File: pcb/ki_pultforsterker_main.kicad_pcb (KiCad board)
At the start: 2 copper layers, 180 x 100 mm, 243 parts, among them J1 24V IN, J10 LED-RINGER, J11 PC1, J12 PC2, J13 TFT, J15 USB1, J16 USB2, J17 USB3, J18 USB4, J19 USB PI, J2 SPK L, J20 AUX2, J21 PWR BAK, J22 EXP, J23 HODETLF, J3 SPK R, J4 AUX1, J5 RPi 40-pin, J6 5V -> PI, J7 KNAPPER, J8 ENCODER, J9 OLED, K1 SRD-05VDC-SL-C, Q10 AO3401A, Q2 AO3400A, Q3 AO3400A, Q4 AO3400A, Q5 AO3400A, Q6 AO3400A, Q7 AO3400A, Q8 AO3401A, Q9 AO3400A, U1 TPS54560BDDA, U10 PCM1808PW, U11 PCM2900CDB, U12 MCP23017-E/SS, U13 TPA6132A2RTER, U2 AMS1117-3.3, U3 LM2662MX, U4 PCM5102APW, U5 PGA2311UA, U6 TPA3116D2DAD, U7 FE1.1s, U8 TS3USB221, U9 AMS1117-3.3, X1 12.288MHz, Y1 12MHz, Y2 12MHz

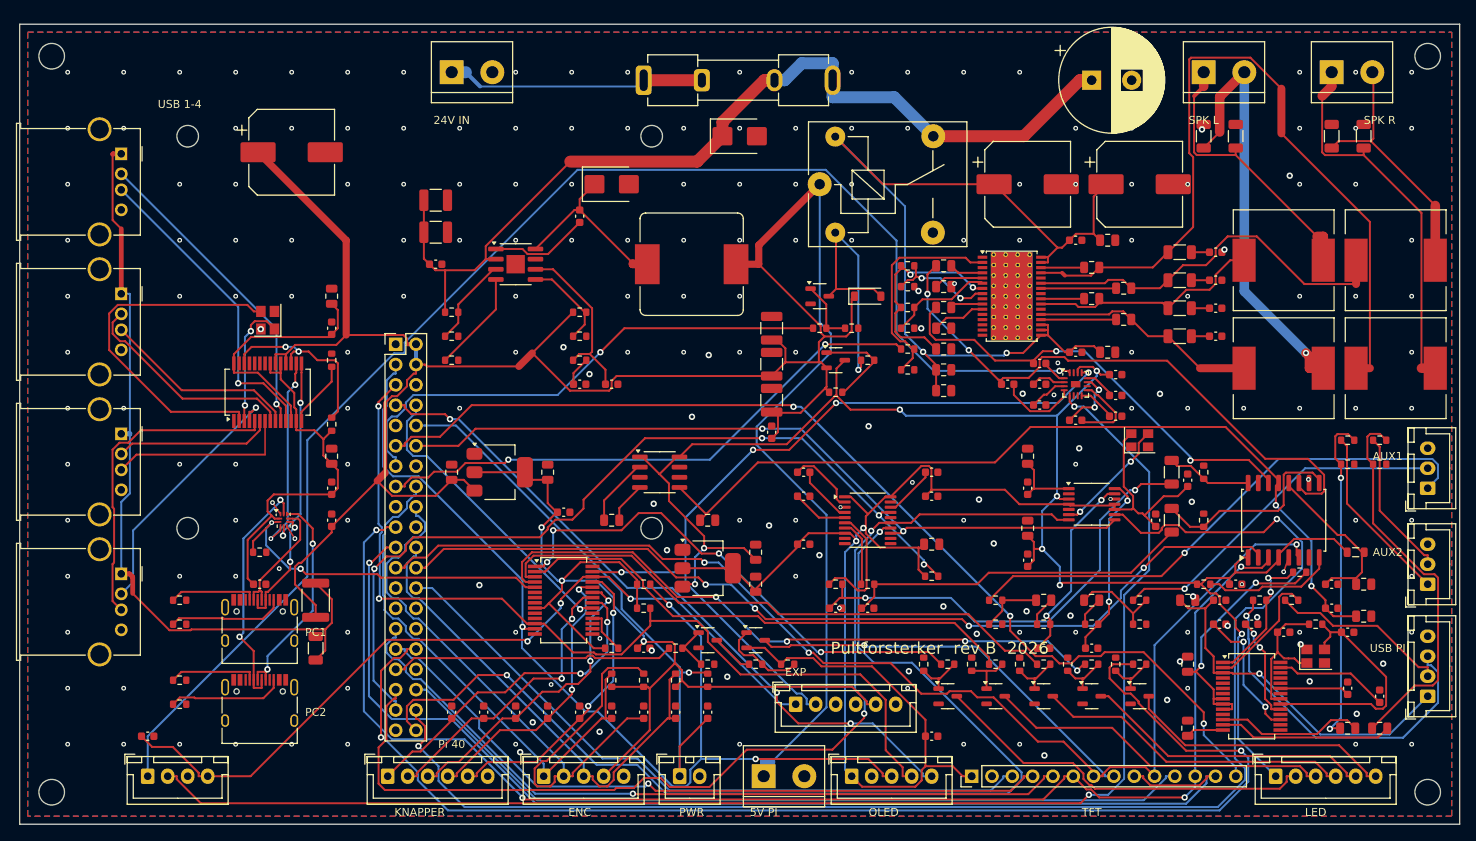
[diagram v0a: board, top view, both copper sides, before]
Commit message: PCB rev B: endelig ruting, gerbere, BOM og DRC etter sikkerhetsgjennomgang
DRC: ingen klaringsfeil, ingen ukoblede nett, alle GND-pads koblet, jordplanet i én del (186 stitching-/bro-vias).
Gjenstår bare silk-advarsler og små courtyard-overlapp.

Co-Authored-By: Claude Fable 5.1 <noreply@anthropic.com>
Claude-Session: https://claude.ai/code/session_01FaJKmYinw8SWRobKXBRYpt
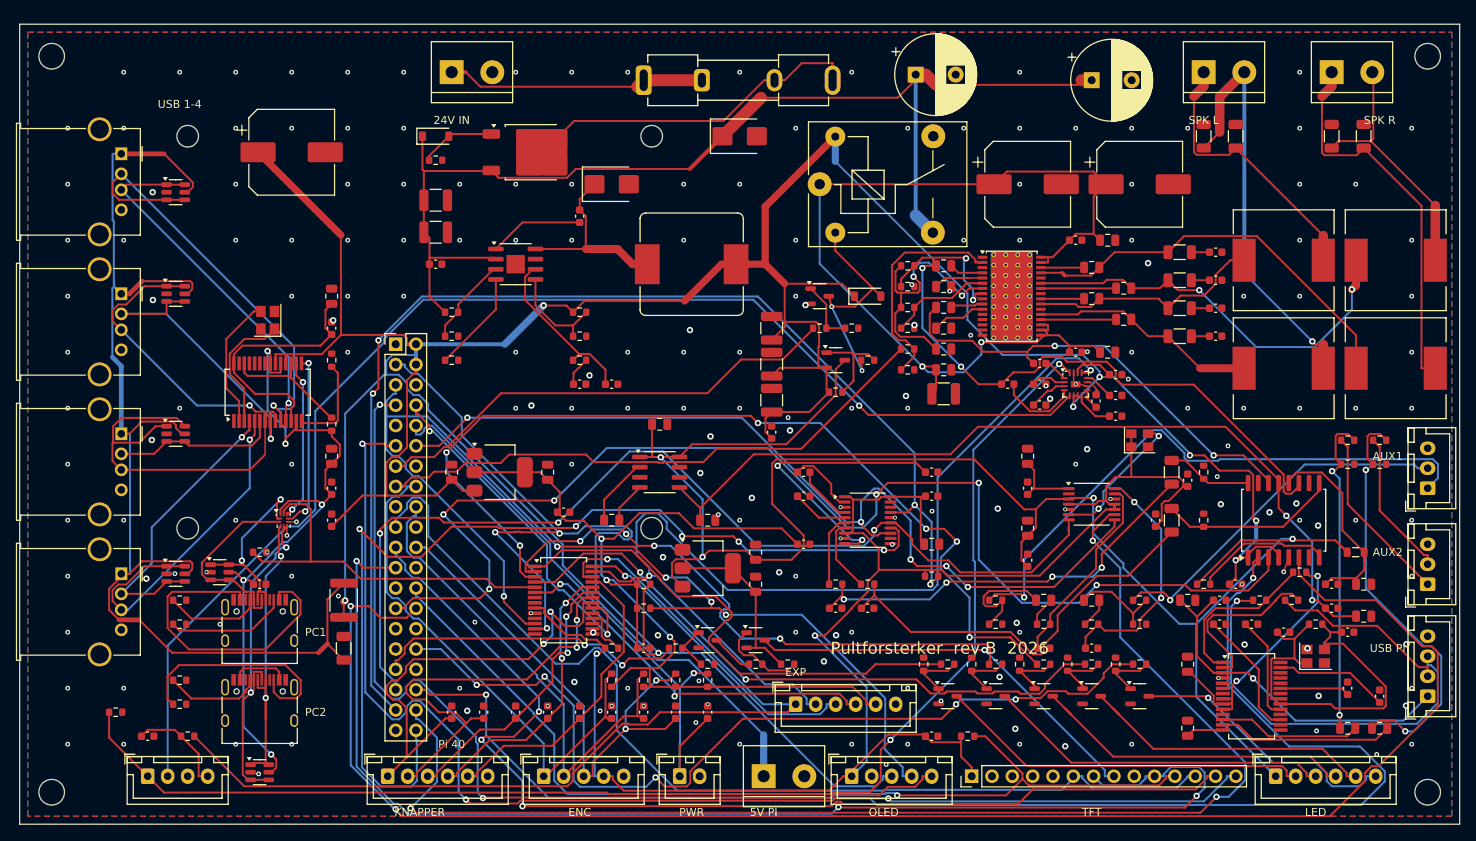
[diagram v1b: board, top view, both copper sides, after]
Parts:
- added C109: 10u, C_0805_2012Metric, F.Cu at (80.0, 50.0)
- added C110: 1000u/35V h<=16, CP_Radial_D10.0mm_P5.00mm, F.Cu at (112.0, 6.30)
- added D10: USBLC6-2SC6, SOT-23-6, F.Cu at (25.0, 68.5)
- added D11: USBLC6-2SC6, SOT-23-6, F.Cu at (30.0, 93.5)
- added D5: BZT52C12 12V, D_SOD-123, F.Cu at (52.0, 14.0)
- added D6: USBLC6-2SC6, SOT-23-6, F.Cu at (19.5, 21.0)
- added D7: USBLC6-2SC6, SOT-23-6, F.Cu at (19.5, 33.7)
- added D8: USBLC6-2SC6, SOT-23-6, F.Cu at (19.5, 51.2)
- added D9: USBLC6-2SC6, SOT-23-6, F.Cu at (19.5, 68.7)
- added Q11: P-MOSFET 60V 20A (AOD409), TO-252-2, F.Cu at (64.0, 16.0)
- added R76: 10k, R_0603_1608Metric, F.Cu at (12.0, 86.0)
- added R77: 10k, R_0603_1608Metric, F.Cu at (21.0, 89.0)
- added R78: 10k, R_0603_1608Metric, F.Cu at (118.5, 89.0)
- added R79: 100k, R_0603_1608Metric, F.Cu at (52.0, 17.0)
- C1: value 2200u/35V -> 1000u/35V h<=16; footprint CP_Radial_D13.0mm_P5.00mm -> CP_Radial_D10.0mm_P5.00mm
- C43: value 10u/50V -> 4.7u/50V; footprint C_0805_2012Metric -> C_1210_3225Metric
- D1: value SMBJ33A -> SMBJ28A
- R1: value 150k -> 330k
- R4: value 53.6k -> 56k
- U1: value TPS54560BDDA -> TPS54560DDAR
- U10: value PCM1808PW -> PCM1808PWR
- U4: value PCM5102APW -> PCM5102APWR
- U6: value TPA3116D2DAD -> TPA3116D2DADR
- U8: value TS3USB221 -> TS3USB221RSER
- moved C103 3.50 mm to (134.6, 47.1), turned to -90 degrees
- moved C71 3.50 mm to (40.5, 78.0)
- moved F2 3.50 mm to (40.5, 72.0)
- moved C43 0.40 mm to (115.5, 46.2)
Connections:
- C100 pad 1: 5V_SW -> 5V
- C108 pad 1: EXP_A5 -> HP_DET
- C20 pad 1: 3V3_SW -> 3V3
- C21 pad 1: 3V3_SW -> 3V3
- C22 pad 1: 3V3_SW -> 3V3
- C27 pad 1: 5V_SW -> 5V
- C77 pad 1: 3V3_SW -> 3V3
- C82 pad 1: 3V3_SW -> 3V3
- C99 pad 1: 3V3_SW -> 3V3
- F1 pad 2: VIN24 -> 24V_F
- J11 pad A4: (no net) -> PC1_VBUS
- J11 pad A9: (no net) -> PC1_VBUS
- J11 pad B4: (no net) -> PC1_VBUS
- J11 pad B9: (no net) -> PC1_VBUS
- J12 pad A4: (no net) -> PC2_VBUS
- J12 pad A9: (no net) -> PC2_VBUS
- J12 pad B4: (no net) -> PC2_VBUS
- J12 pad B9: (no net) -> PC2_VBUS
- J13 pad 1: 3V3_SW -> 3V3
- J13 pad 3: TFT_CS -> (no net)
- J13 pad 4: TFT_RST -> (no net)
- J13 pad 5: TFT_DC -> (no net)
- J13 pad 9: SPI_MISO -> (no net)
- J22 pad 3: (no net) -> EXP_A7
- J22 pad 4: (no net) -> EXP_B5
- J22 pad 6: (no net) -> GND
- J23 pad 4: EXP_A5 -> HP_DET
- J5 pad 24: SPI_CS -> (no net)
- J5 pad 26: TFT_CS -> TOUCH_CS
- J5 pad 27: (no net) -> PGA_SDI
- J5 pad 28: (no net) -> PGA_SCLK
- J5 pad 29: TFT_DC -> (no net)
- J5 pad 31: TFT_RST -> (no net)
- J5 pad 36: TOUCH_CS -> PGA_CS
- J9 pad 1: 3V3_SW -> 3V3
- K1 pad 1: 5V -> 24V_AMP
- K1 pad 3: (no net) -> VIN24
- K1 pad 4: VIN24 -> (no net)
- K1 pad 5: 24V_AMP -> 5V
- R7 pad 1: 3V3_SW -> 3V3
- U10 pad 10: 3V3_SW -> 3V3
- U10 pad 11: 3V3_SW -> 3V3
- U10 pad 4: 3V3_SW -> 3V3
- U12 pad 28: (no net) -> EXP_A7
- U12 pad 6: (no net) -> EXP_B5
- U13 pad 14: 5V_SW -> 5V
- U13 pad 6: GND -> 5V
- U13 pad 7: GND -> 5V
- U4 pad 1: 3V3_SW -> 3V3
- U4 pad 10: GND -> DAC_LDOO
- U4 pad 18: DAC_LDOO -> GND
- U4 pad 20: 3V3_SW -> 3V3
- U4 pad 8: 3V3_SW -> 3V3
- U5 pad 1: 5V_SW -> 5V
- U5 pad 2: SPI_CS -> PGA_CS
- U5 pad 3: SPI_MOSI -> PGA_SDI
- U5 pad 4: 5V_SW -> 5V
- U5 pad 6: SPI_SCLK -> PGA_SCLK
- U8 pad 1: USB_VD33 -> PC1_DP
- U8 pad 10: GND -> USB_VD33
- U8 pad 2: USB_SEL -> PC1_DM
- U8 pad 3: USB_UP_DP -> PC2_DP
- U8 pad 4: USB_UP_DM -> PC2_DM
- U8 pad 6: PC1_DP -> GND
- U8 pad 7: PC1_DM -> USB_UP_DM
- U8 pad 8: PC2_DP -> USB_UP_DP
- U8 pad 9: PC2_DM -> USB_SEL
- X1 pad 1: (no net) -> 3V3
- X1 pad 4: 3V3_SW -> 3V3
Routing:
- net 3V3: track 128.3 -> 336.3 mm, vias 3 -> 5
- net PGA_SCLK: track 0.00 -> 204.2 mm, vias 0 -> 2
- net PGA_CS: track 0.00 -> 174.4 mm, vias 0 -> 2
- net 3V3_SW: track 190.2 -> 22.6 mm, vias 2 -> 0
- net PGA_SDI: track 0.00 -> 154.7 mm, vias 0 -> 6
- net 5V: track 313.9 -> 433.9 mm, vias 0 -> 7
- net SPI_CS: track 115.7 -> 0.00 mm, vias 4 -> 0
- net TFT_DC: track 95.8 -> 0.00 mm, vias 1 -> 0
- net TFT_RST: track 89.0 -> 0.00 mm, vias 1 -> 0
- net TFT_CS: track 85.9 -> 0.00 mm
- net 5V_USB: track 97.5 -> 149.7 mm
- net 24V_F: track 0.00 -> 50.5 mm
- net EXP_B5: track 0.00 -> 47.6 mm, vias 0 -> 2
- net OUTPR: track 97.3 -> 50.8 mm
- net LED_PWR_G: track 157.3 -> 111.9 mm, vias 2 -> 5
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
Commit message: PCB rev B: endelig ruting med GND som rutet nett + plan, NTC-overtemperaturvakt, gerbere/BOM/DRC
DRC: 0 klaringsfeil, 0 hullfeil, 0 ukoblede, jordplanet i én del. Gjenstår silk-advarsler og små courtyard-overlapp.

Co-Authored-By: Claude Fable 5.1 <noreply@anthropic.com>
Claude-Session: https://claude.ai/code/session_01FaJKmYinw8SWRobKXBRYpt
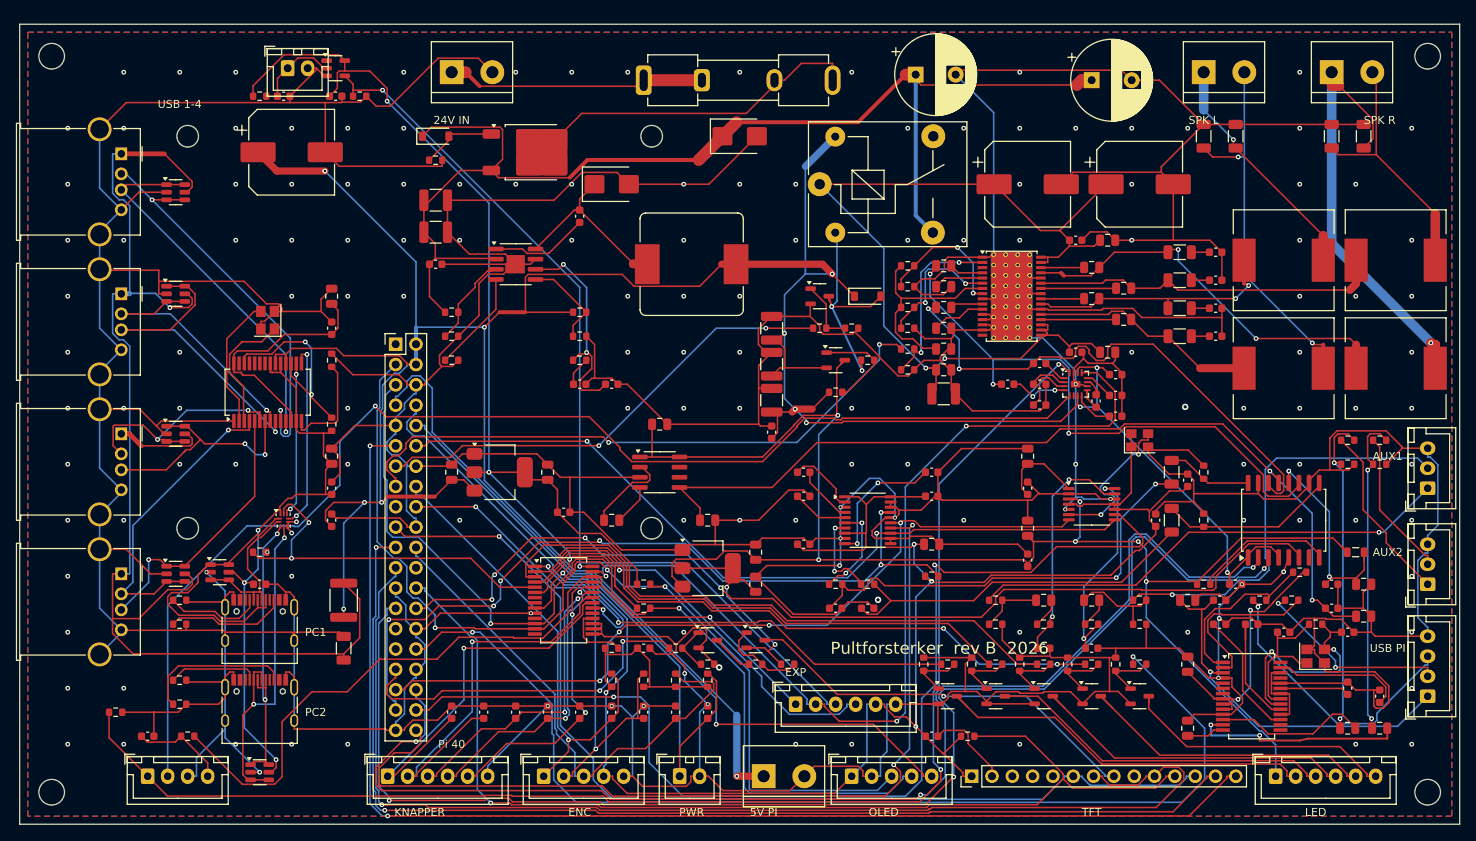
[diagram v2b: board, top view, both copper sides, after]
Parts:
- added C111: 100n, C_0603_1608Metric, F.Cu at (39.5, 9.00)
- added C112: 100n, C_0603_1608Metric, F.Cu at (33.0, 9.00)
- added J24: NTC, JST_XH_B2B-XH-A_1x02_P2.50mm_Vertical, F.Cu at (33.5, 5.50)
- added R81: 3.3k, R_0603_1608Metric, F.Cu at (30.0, 9.00)
- added R82: 100k, R_0603_1608Metric, F.Cu at (42.5, 9.00)
- added U14: 74LVC1G14, SOT-23-5, F.Cu at (39.5, 5.50)
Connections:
- J11 pad A4: PC1_VBUS -> PC1_VBUS_A
- J11 pad A9: PC1_VBUS -> PC1_VBUS_B
- J11 pad B4: PC1_VBUS -> PC1_VBUS_B
- J11 pad B9: PC1_VBUS -> PC1_VBUS_A
- J12 pad A4: PC2_VBUS -> PC2_VBUS_A
- J12 pad A9: PC2_VBUS -> PC2_VBUS_B
- J12 pad B4: PC2_VBUS -> PC2_VBUS_B
- J12 pad B9: PC2_VBUS -> PC2_VBUS_A
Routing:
- net GND: track 6.18 -> 1674.6 mm, vias 204 -> 154
- net EXP_A7: track 38.8 -> 117.5 mm, vias 1 -> 2
- net PGA_SCLK: track 204.2 -> 125.8 mm, vias 2 -> 4
- net DAC_XSMT: track 147.4 -> 97.4 mm, vias 4 -> 6
- net 3V3: track 336.3 -> 386.0 mm, vias 5 -> 8
- net LED_AUX_G: track 117.1 -> 75.3 mm, vias 6 -> 0
- net PC1_VBUS: track 39.7 -> 0.00 mm
- net I2S_ADC: track 163.7 -> 135.1 mm, vias 3 -> 2
- net I2S_LRCK: track 125.3 -> 99.9 mm, vias 3 -> 4
- net OLED_RES: track 120.2 -> 95.6 mm, vias 2 -> 1
- net 5V_SW: track 221.6 -> 198.2 mm, vias 4 -> 6
- net LED_PWR_G: track 111.9 -> 134.9 mm, vias 5 -> 2
- net DAC_LDOO: track 35.9 -> 16.7 mm
- net EXP_A5: track 119.8 -> 101.4 mm
- net 5V: track 433.9 -> 416.0 mm, vias 7 -> 13
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
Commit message: PCB rev B: ferdig rutet – DRC uten klarings-, kortslutnings-, kant- eller koblingsfeil
Full ny Freerouting-kjøring med låst strømskinne (24 V inn → sikring → Q11 → relé → TPA3116,
5 V buck → C8–C11 → J6/Pi-header). Flaskehalser: 24V_IN 2,0, 24V_F 1,85, VIN24 1,0, 5 V til Pi 1,5 mm.
Gjenstår i DRC: kun silk/courtyard-varsler, 11 «starved thermal» på THT-GND-pads som også har rutet GND-spor,
og 199 bibliotekmeldinger (footprints er innebygd).

Co-Authored-By: Claude Fable 5.1 <noreply@anthropic.com>
Claude-Session: https://claude.ai/code/session_01FaJKmYinw8SWRobKXBRYpt
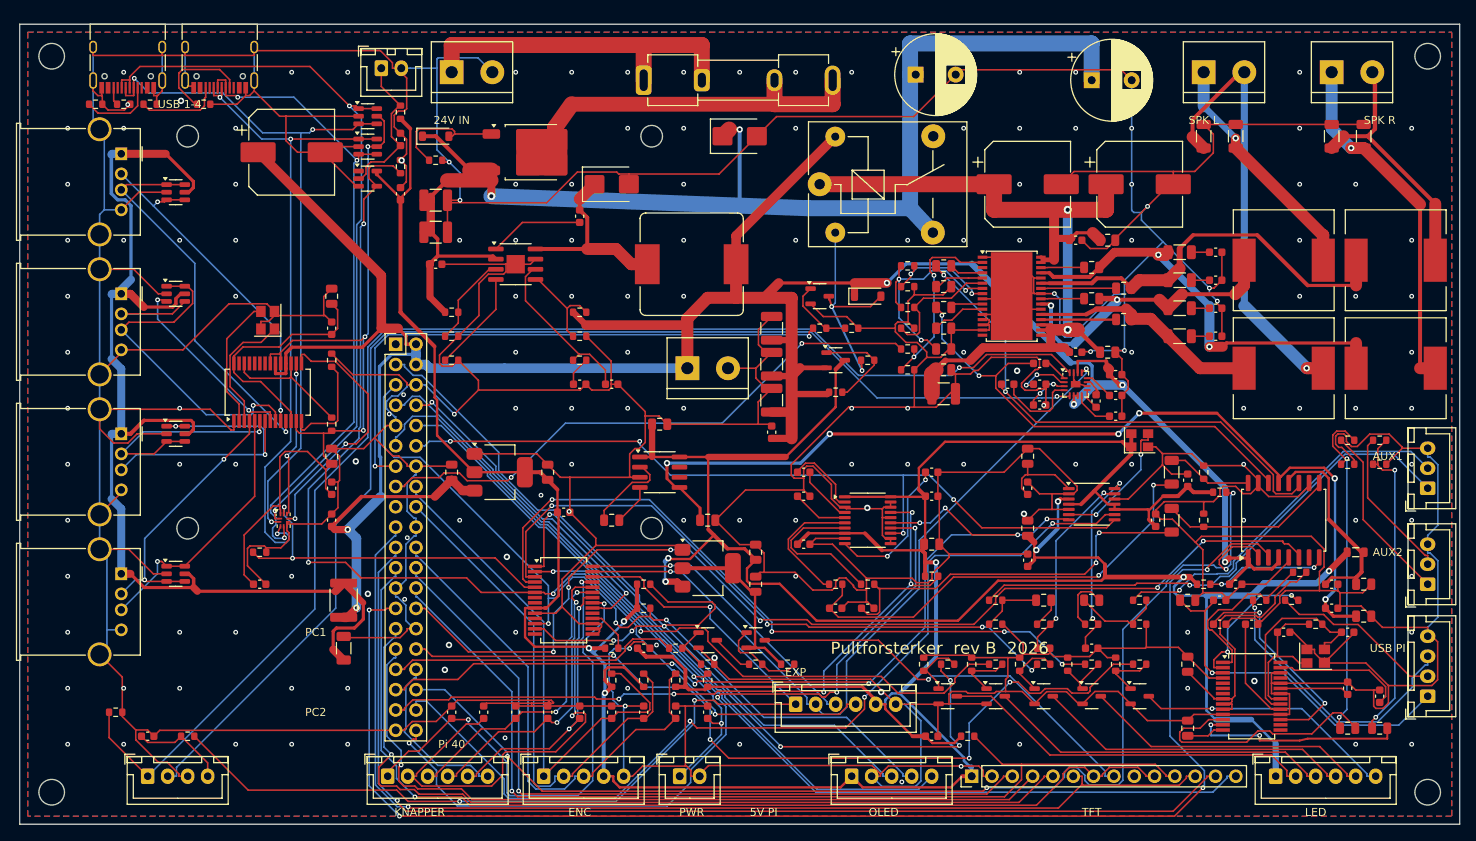
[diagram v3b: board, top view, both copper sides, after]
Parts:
- added R83: 10k, R_0603_1608Metric, F.Cu at (150.0, 58.5)
- U6: footprint HTSSOP-32-1EP_6.1x11mm_P0.65mm_EP5.2x11mm_Mask4.11x4.36mm_ThermalVias -> HTSSOP-32-1EP_6.1x11mm_P0.65mm_EP5.2x11mm_Mask4.11x4.36mm
- moved J12 82.3 mm to (25.0, 3.90), turned to 180 degrees
- moved D11 79.4 mm to (43.5, 15.3)
- moved R51 75.1 mm to (16.3, 10.0)
- moved J11 74.0 mm to (13.5, 3.90), turned to 180 degrees
- moved R50 72.1 mm to (23.0, 10.0)
- moved R49 65.4 mm to (13.0, 10.0)
- moved R48 62.9 mm to (9.50, 10.0)
- moved D10 59.9 mm to (43.5, 11.5)
- moved J6 51.9 mm to (83.5, 43.0)
- moved R81 17.7 mm to (47.6, 11.0), turned to 90 degrees
- moved C112 15.6 mm to (47.6, 14.4), turned to 90 degrees
- moved C111 14.6 mm to (47.6, 21.2), turned to 90 degrees
- moved U14 14.4 mm to (43.5, 19.3)
- moved J24 11.7 mm to (45.2, 5.50)
- moved R82 10.2 mm to (47.6, 17.8), turned to 90 degrees
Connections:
- J13 pad 3: (no net) -> TFT_CS
- J13 pad 4: (no net) -> TFT_RST
- J13 pad 5: (no net) -> TFT_DC
- J5 pad 24: (no net) -> TFT_CS
- J5 pad 29: (no net) -> TFT_DC
- J5 pad 31: (no net) -> TFT_RST
- R82 pad 1: EXP_A7 -> EXP_B5
- U14 pad 4: EXP_A7 -> EXP_B5
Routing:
- net GND: track 1674.6 -> 1815.2 mm, vias 154 -> 157
- net TFT_DC: track 0.00 -> 107.8 mm, vias 0 -> 1
- net TFT_RST: track 0.00 -> 99.4 mm, vias 0 -> 1
- net TFT_CS: track 0.00 -> 96.2 mm, vias 0 -> 1
- net EXP_B5: track 53.1 -> 137.7 mm, vias 1 -> 4
- net EXP_A7: track 117.5 -> 37.8 mm, vias 2 -> 1
- net PC1_DM: track 20.4 -> 89.2 mm, vias 0 -> 3
- net PC1_DP: track 35.5 -> 94.2 mm, vias 0 -> 2
- net 5V: track 416.0 -> 360.0 mm, vias 13 -> 6
- net PC2_DP: track 37.4 -> 82.2 mm, vias 2 -> 3
- net PC2_DM: track 44.2 -> 81.7 mm, vias 2 -> 3
- net TOUCH_IRQ: track 159.0 -> 128.5 mm, vias 2 -> 0
- net USB_VD33: track 73.6 -> 102.0 mm
- net LED_PWR_G: track 134.9 -> 106.9 mm, vias 2 -> 4
- net LED_AIR_G: track 56.5 -> 82.9 mm, vias 2 -> 4
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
